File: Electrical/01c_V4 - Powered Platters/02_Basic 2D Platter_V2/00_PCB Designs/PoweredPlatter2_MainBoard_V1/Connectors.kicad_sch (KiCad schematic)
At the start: 4 parts, among them J1 Conn_01x08, J2 Conn_01x08, J4 Conn_01x03

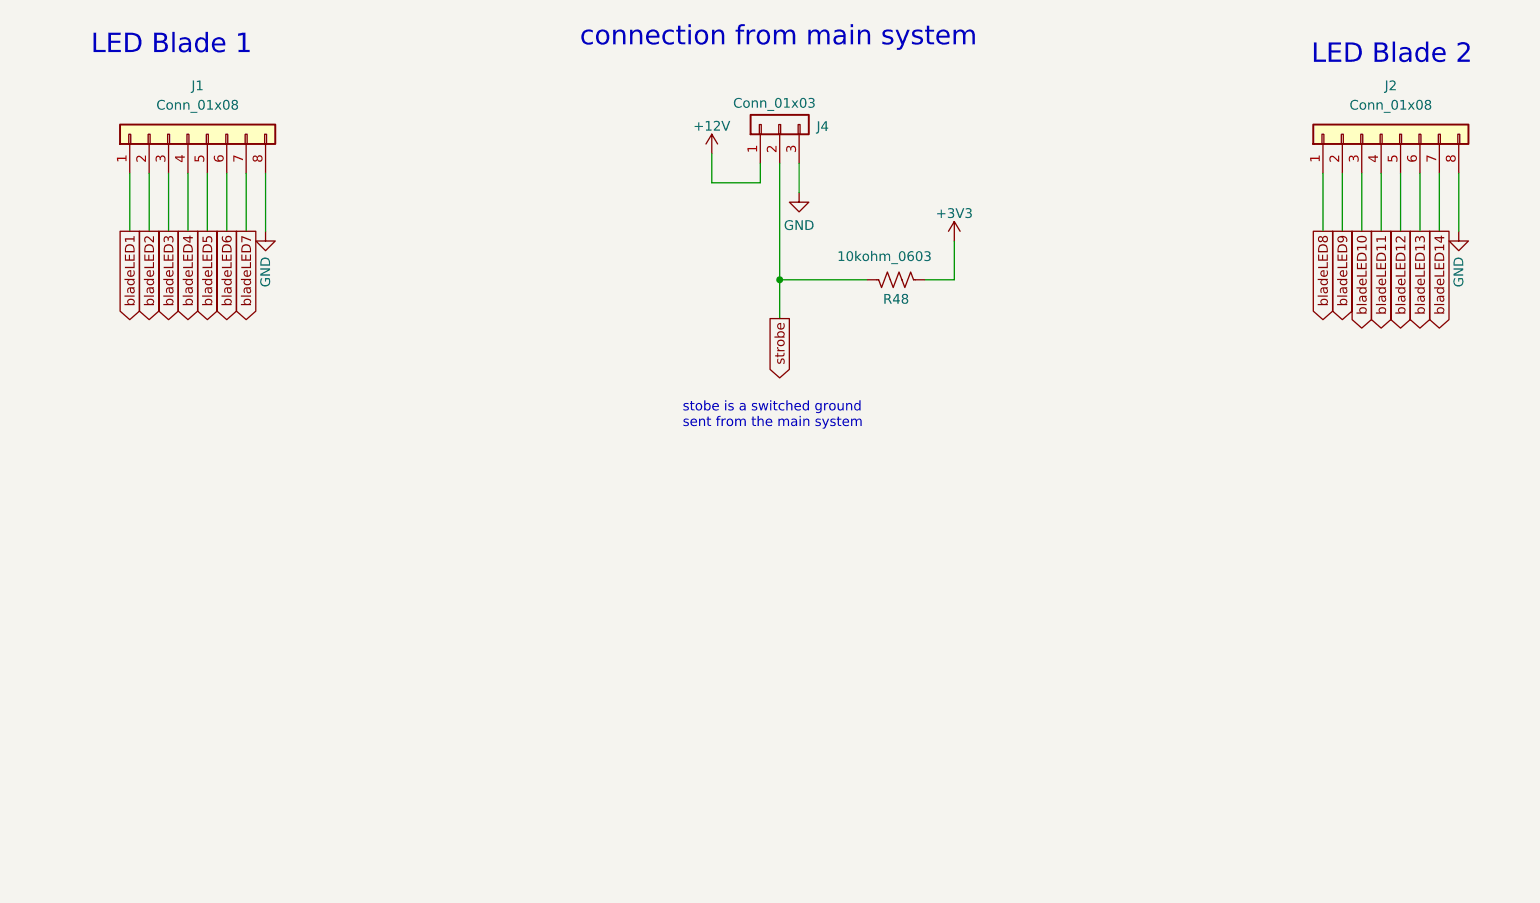
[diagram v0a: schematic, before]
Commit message: second powered platter main PCB designed and ready for CNC milling
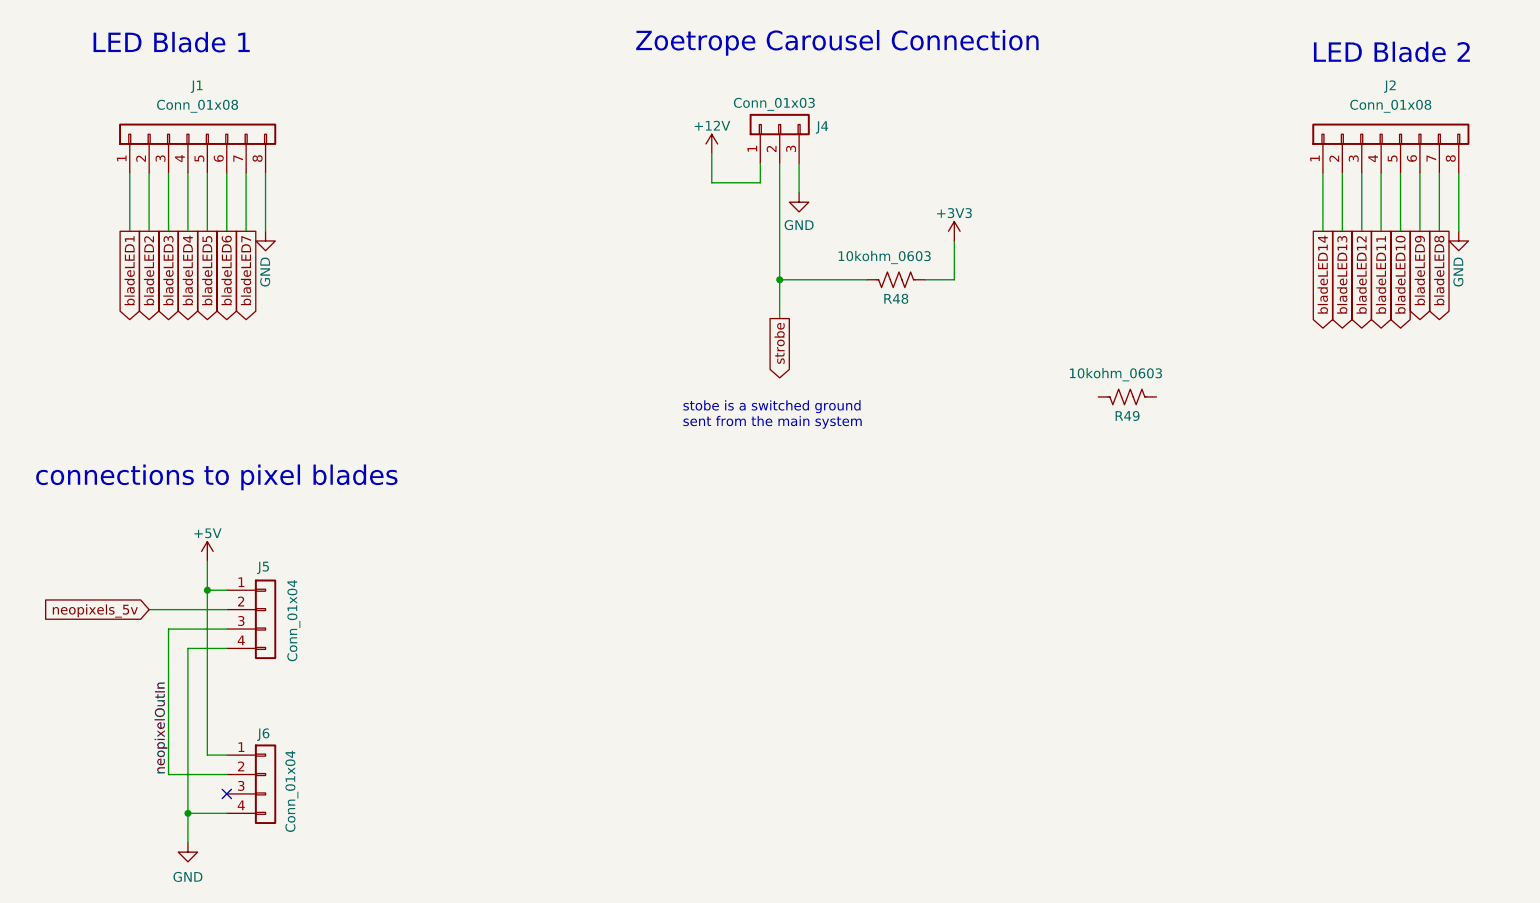
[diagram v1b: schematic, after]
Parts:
- added J5, J6: Conn_01x04, Connector_PinHeader_2.54mm:PinHeader_1x04_P2.54mm_Vertical, symbol Connector_Generic:Conn_01x04
- added R49: 10kohm_0603, Resistor_SMD:R_0603_1608Metric, symbol Device:R_US
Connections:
- net GND: now also J5.4 (Pin_4), J6.4 (Pin_4)
- net bladeLED10: now also J2.5 (Pin_5); no longer J2.3 (Pin_3)
- net bladeLED12: now also J2.3 (Pin_3); no longer J2.5 (Pin_5)
- net bladeLED13: now also J2.2 (Pin_2); no longer J2.6 (Pin_6)
- net bladeLED14: now also J2.1 (Pin_1); no longer J2.7 (Pin_7)
- net bladeLED8: now also J2.7 (Pin_7); no longer J2.1 (Pin_1)
- net bladeLED9: now also J2.6 (Pin_6); no longer J2.2 (Pin_2)
- new net +5V: J5.1 (Pin_1), J6.1 (Pin_1)
- new net neopixelOutIn: J5.3 (Pin_3), J6.2 (Pin_2)
- new net neopixels_5v: J5.2 (Pin_2)
- no-connect marks 0 -> 1
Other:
- note added: "Zoetrope Carousel Connection"
- note added: "connections to pixel blades"
- note removed: "connection from main system"
